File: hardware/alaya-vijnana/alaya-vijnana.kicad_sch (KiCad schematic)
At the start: 0 parts

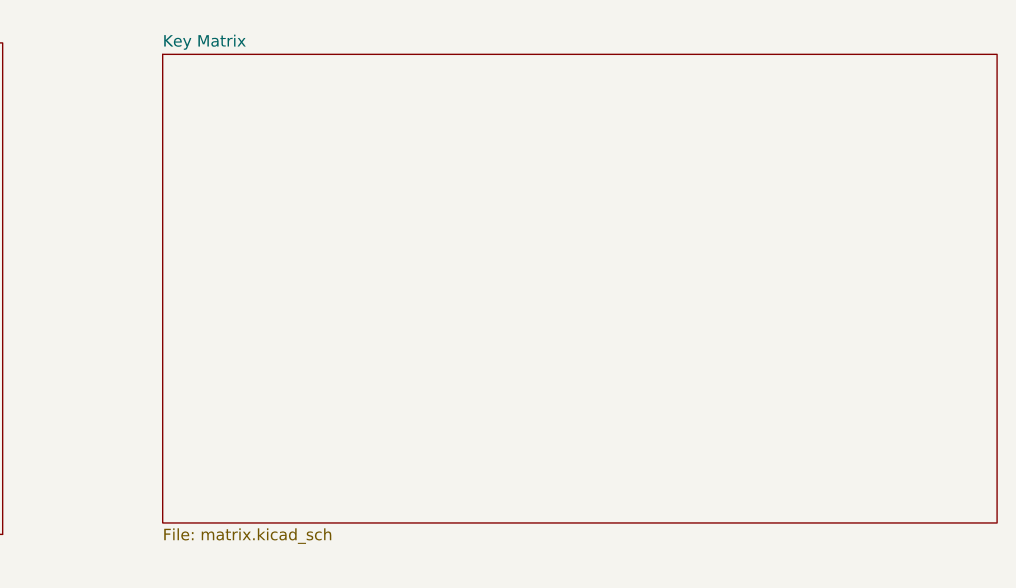
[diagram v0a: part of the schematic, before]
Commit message: left side wired up
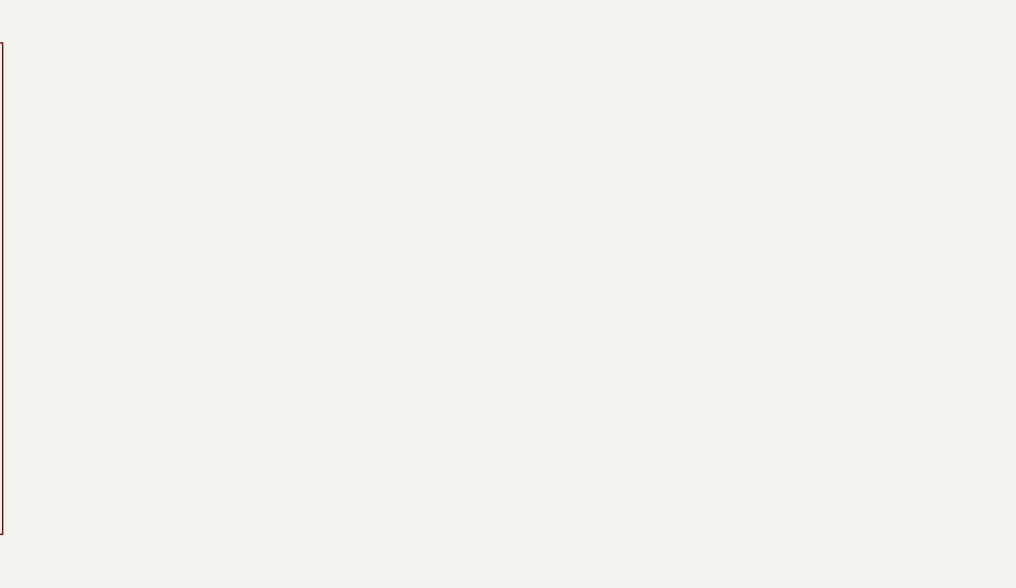
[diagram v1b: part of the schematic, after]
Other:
- removed sheet Key Matrix
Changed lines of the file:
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@@
-		)
-	)
-	(sheet
-		(at 245.11 36.83)
-		(size 92.71 52.07)
-		(exclude_from_sim no)
-		(in_bom yes)
-		(on_board yes)
-		(dnp no)
-		(fields_autoplaced yes)
-		(stroke
-			(width 0.1524)
-			(type solid)
-		)
-		(fill
-			(color 0 0 0 0.0000)
-		)
-		(property "Sheetname" "Key Matrix"
-			(at 245.11 36.1184 0)
-			(effects
-				(font
-					(size 1.27 1.27)
-				)
-				(justify left bottom)
-			)
-		)
-		(property "Sheetfile" "matrix.kicad_sch"
-			(at 245.11 89.4846 0)
-			(effects
-				(font
-					(size 1.27 1.27)
-				)
-				(justify left top)
-			)
-		)
-		(instances
-			(project "alaya-vijnana"
-				(path "/a3984b5f-5482-487c-827c-93986b80e1c8"
-					(page "4")
-				)
-			)
 		)
 	)
